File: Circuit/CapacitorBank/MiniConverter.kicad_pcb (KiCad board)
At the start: 2 copper layers, 66 x 22.9 mm, 10 parts, among them J1 AC Power In, J2 To Capacitors, T1 6:75+75

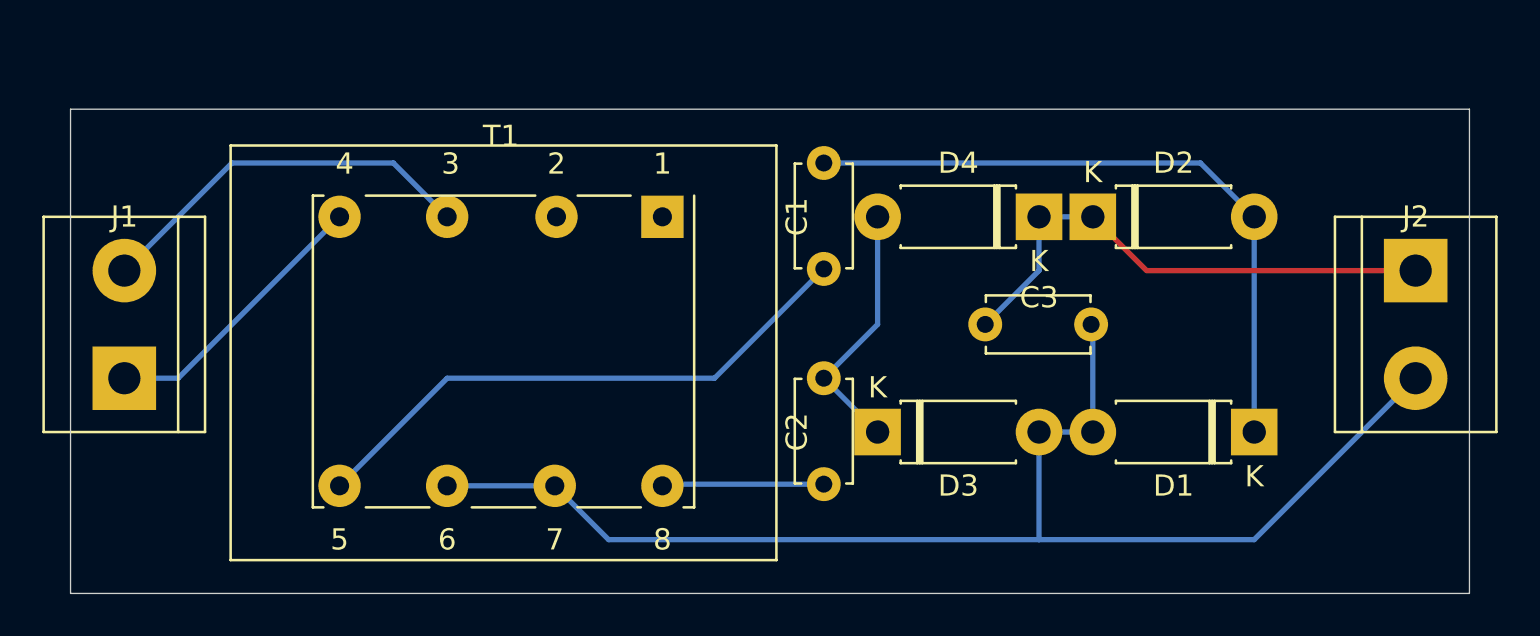
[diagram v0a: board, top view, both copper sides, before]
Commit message: [Circuit] Add mini converter module for mini capacitor bank
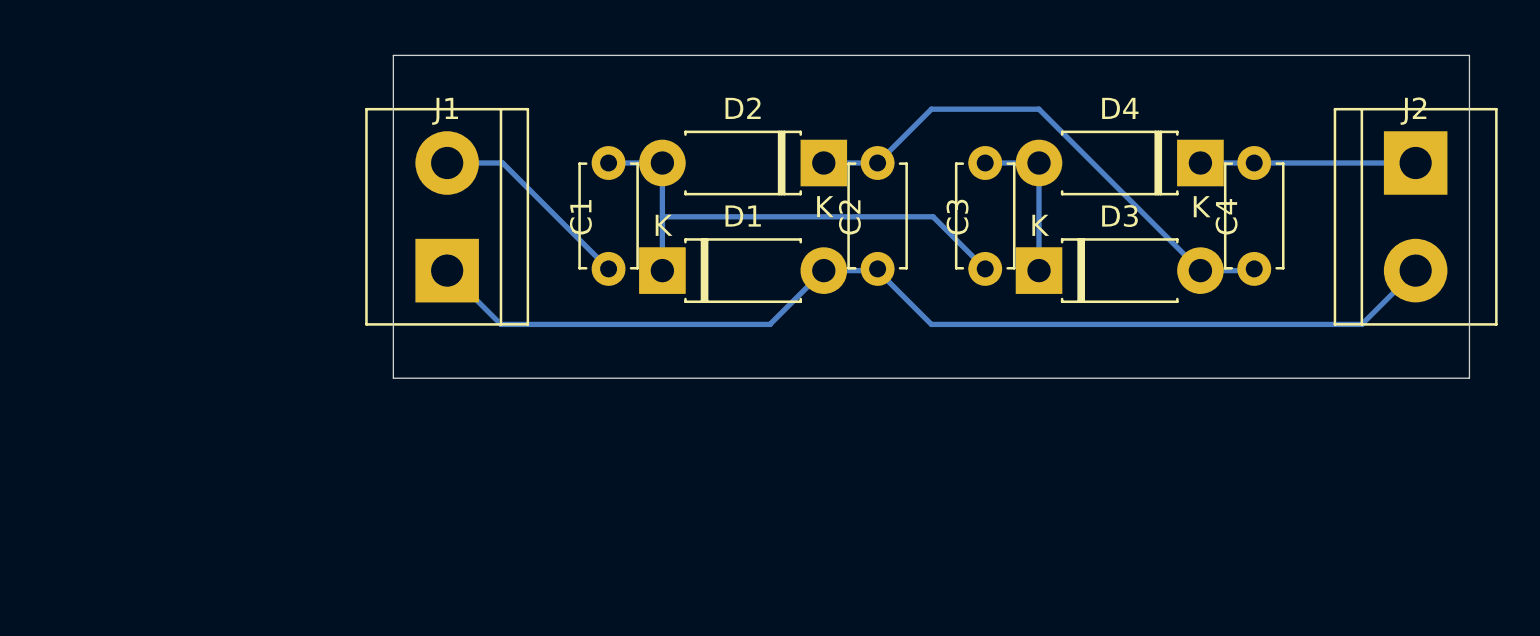
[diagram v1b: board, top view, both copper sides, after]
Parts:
- removed the C2 at (132.1, 68.6)
- removed T1: 6:75+75, Power:Transformer_Generic_EE25_8Pin
- added C3: 1nF, Capacitor_THT:C_Disc_D4.7mm_W2.5mm_P5.00mm, F.Cu at (139.7, 58.4)
- added C4: 1nF, Capacitor_THT:C_Disc_D4.7mm_W2.5mm_P5.00mm, F.Cu at (152.4, 58.4)
- moved D1 29.0 mm to (124.5, 63.5), turned to 0 degrees
- moved J1 16.1 mm to (114.3, 63.5)
- moved D2 13.0 mm to (132.1, 58.4), turned to 180 degrees
- moved D3 10.8 mm to (142.2, 63.5)
- moved C1 10.2 mm to (121.9, 58.4)
- moved C2 9.16 mm to (134.6, 58.4), turned to 270 degrees
- moved D4 8.03 mm to (149.9, 58.4)
- moved J2 5.08 mm to (160.0, 58.4)
- renumbered C3 to C2
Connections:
- C1 pad 2: Net-(C1-Pad2) -> /ACPowerIn+
- C2 pad 1: /CapacitorPower+ -> Net-(C2-Pad1)
- C2 pad 2: /CapacitorPower- -> /ACPowerIn-
- D1 pad 2: /CapacitorPower- -> /ACPowerIn-
- D2 pad 1: /CapacitorPower+ -> Net-(C2-Pad1)
- D3 pad 2: /CapacitorPower- -> Net-(C2-Pad1)
- J2 pad 2: /CapacitorPower- -> /ACPowerIn-
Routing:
- net /CapacitorPower-: track 62.7 -> 0.00 mm
- net /ACPowerIn-: track 13.3 -> 50.0 mm
- net Net-(C1-Pad2): track 27.1 -> 0.00 mm
- net Net-(C2-Pad1): track 0.00 -> 24.6 mm
- net /CapacitorPower+: track 25.0 -> 10.2 mm
- net /ACPowerIn+: track 18.4 -> 9.69 mm
- net Net-(C2-Pad2): track 7.65 -> 0.00 mm
- net Net-(C1-Pad1): track 31.5 -> 23.9 mm
- net Net-(C3-Pad1): track 12.3 -> 7.62 mm
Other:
- board size 66 x 22.9 mm -> 50.8 x 15.2 mm

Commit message: [Circuit] Improve the mini converter a little bit
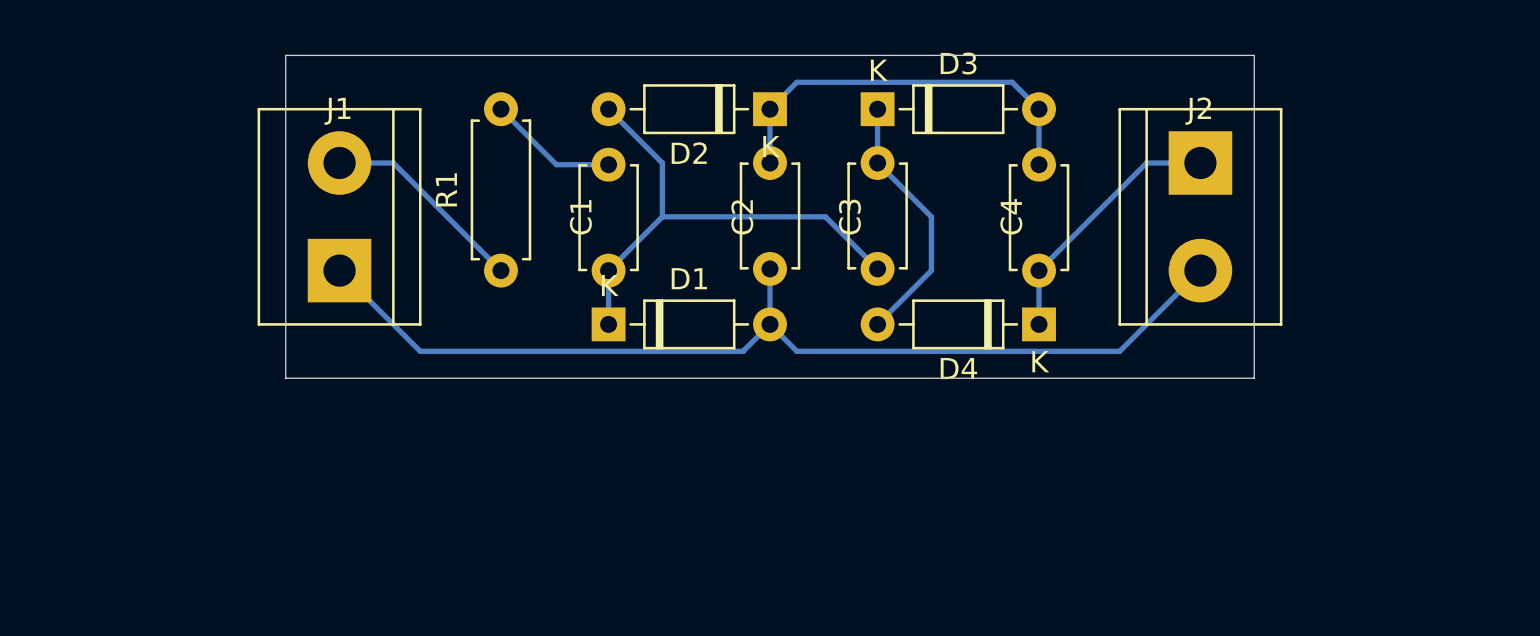
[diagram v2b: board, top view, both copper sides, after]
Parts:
- added R1: 100, Resistor_THT:R_Axial_DIN0207_L6.3mm_D2.5mm_P7.62mm_Horizontal, F.Cu at (116.8, 55.9)
- D1, D2, D3, D4: value 1N4007 -> 1N4148; footprint Diode_THT:D_DO-41_SOD81_P7.62mm_Horizontal -> Diode_THT:D_DO-35_SOD27_P7.62mm_Horizontal
- moved C4 11.4 mm to (142.2, 63.5), turned to 90 degrees
- moved D4 10.8 mm to (142.2, 66.0)
- moved D3 10.8 mm to (134.6, 55.9)
- moved J2 10.2 mm to (149.9, 58.4)
- moved C2 5.08 mm to (129.5, 58.4)
- moved C1 5.08 mm to (121.9, 63.5), turned to 90 degrees
- moved J1 5.08 mm to (109.2, 63.5)
- moved C3 5.08 mm to (134.6, 58.4)
- moved D2 3.59 mm to (129.5, 55.9)
- moved D1 3.59 mm to (121.9, 66.0)
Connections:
- C1 pad 2: /ACPowerIn+ -> Net-(C1-Pad2)
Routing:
- net Net-(C1-Pad2): track 0.00 -> 6.28 mm
- net Net-(C2-Pad1): track 24.6 -> 18.9 mm
- net Net-(C3-Pad1): track 7.62 -> 12.3 mm
- net /ACPowerIn-: track 50.0 -> 47.6 mm
- net /CapacitorPower+: track 10.2 -> 12.3 mm
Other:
- board size 50.8 x 15.2 mm -> 45.7 x 15.2 mm

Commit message: [Circuit] Add isolated switches to bleeder circuits
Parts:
- R1: value 100 -> 220
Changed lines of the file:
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@@
       (effects (font (size 1 1) (thickness 0.15)))
     )
-    (fp_text value 100 (at 2.54 0 90) (layer F.Fab)
+    (fp_text value 220 (at 2.54 0 90) (layer F.Fab)
       (effects (font (size 1 1) (thickness 0.15)))
     )
